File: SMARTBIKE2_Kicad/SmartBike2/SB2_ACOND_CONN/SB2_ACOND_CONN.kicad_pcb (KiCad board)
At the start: 2 copper layers, 45 x 100 mm, 30 parts, among them IC1 ESP32-WROVER-B__8MB_, J1 Conn_01x02, J2 Conn_01x01, J3 Conn_02x03_Counter_Clockwise, J4 Conn_01x04, J5 Conn_01x05, J6 Conn_01x08, J7 Conn_01x08, J8 Conn_01x04, SW1 SW_Boot, SW2 SW_Reset

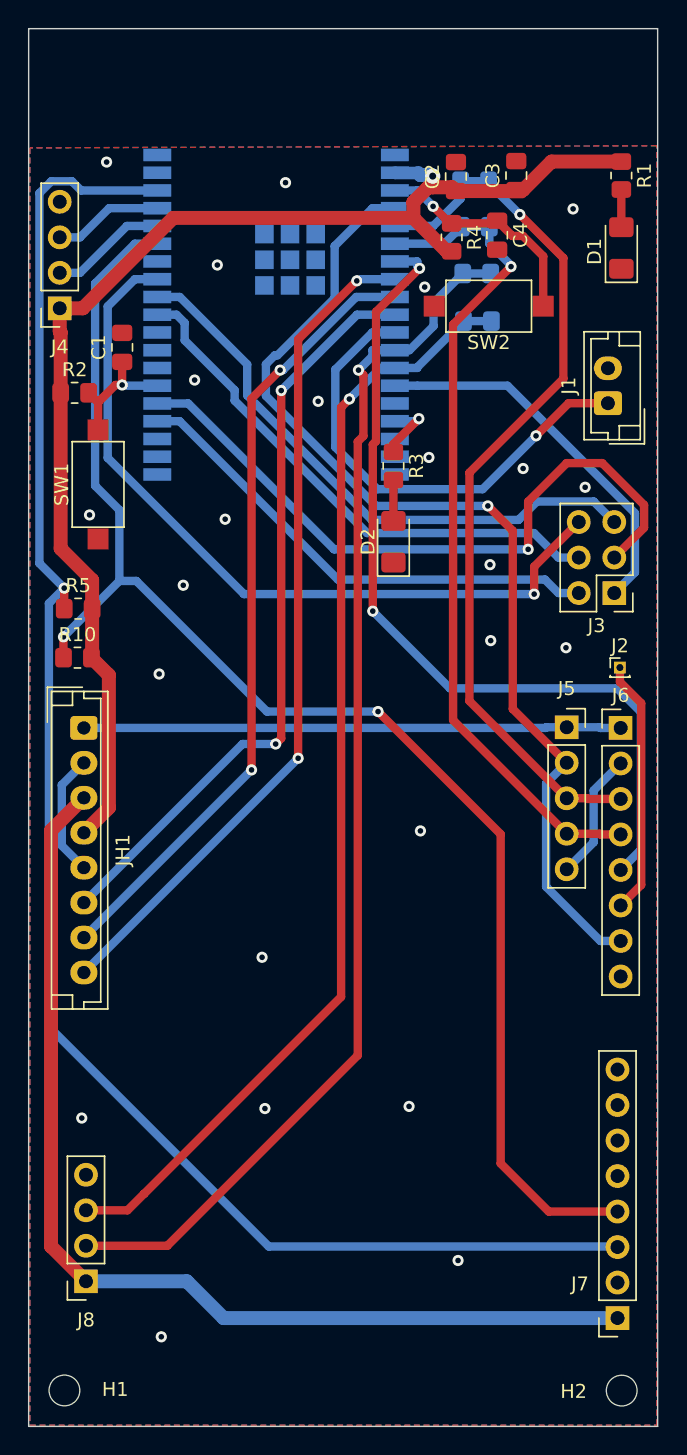
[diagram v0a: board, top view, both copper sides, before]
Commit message: Impresión vías sin metalización
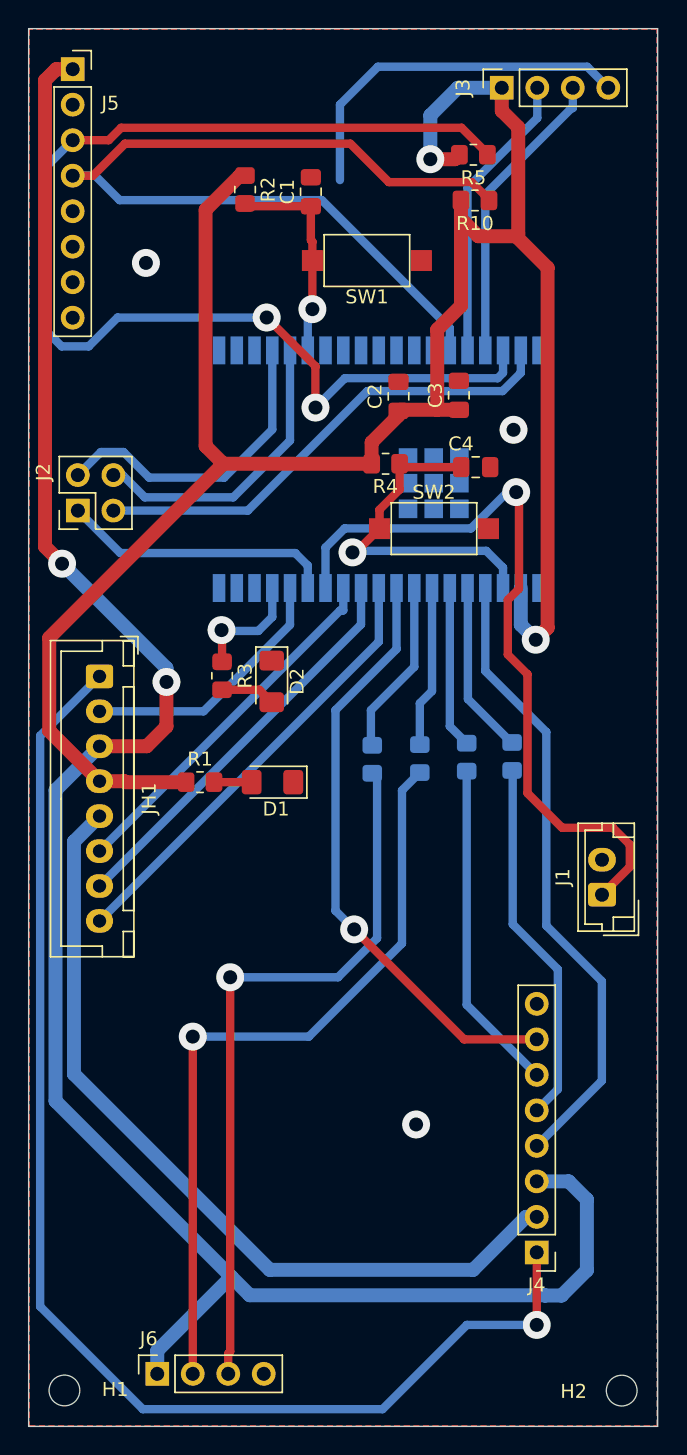
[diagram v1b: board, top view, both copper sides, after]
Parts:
- removed the J3 at (91.9, 65.4)
- removed the J5 at (88.5, 75.0)
- removed the J6 at (92.4, 75.0)
- added J4: Conn_01x08, Connector_PinHeader_2.54mm:PinHeader_1x08_P2.54mm_Vertical, F.Cu at (86.3, 112.5)
- J2: value Conn_01x01 -> Conn_02x02_Counter_Clockwise; footprint Connector_PinHeader_1.00mm:PinHeader_1x01_P1.00mm_Vertical -> Connector_PinHeader_2.54mm:PinHeader_2x02_P2.54mm_Vertical
- JH1: footprint Connector_JST:JST_EH_B8B-EH-A_1x08_P2.50mm_Vertical -> Connector_JST:JST_XH_B8B-XH-A_1x08_P2.50mm_Vertical
- moved J5 97.5 mm to (53.1, 27.9), turned to 0 degrees
- moved R1 52.8 mm to (62.3, 78.9), turned to 0 degrees
- moved D1 45.6 mm to (67.4, 78.9), turned to 180 degrees
- moved R10 43.3 mm to (81.9, 37.3), turned to 180 degrees
- moved R5 43.1 mm to (81.8, 34.0), turned to 180 degrees
- moved R6 41.2 mm to (84.6, 77.1), turned to -90 degrees
- moved J2 40.4 mm to (53.5, 59.5), turned to 90 degrees
- moved R7 38.0 mm to (81.3, 77.1), turned to -90 degrees
- moved J3 35.3 mm to (83.8, 29.2), turned to 90 degrees
- moved J1 35.2 mm to (91.0, 87.0)
- moved R8 34.9 mm to (78.0, 77.2), turned to -90 degrees
- moved R9 32.2 mm to (74.6, 77.3), turned to -90 degrees
- moved SW1 25.0 mm to (74.2, 41.6), turned to 180 degrees
- moved R3 19.4 mm to (63.8, 71.3)
- moved R2 19.0 mm to (65.5, 36.5), turned to -90 degrees
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- renumbered J4 to J3, J7 to J5, J8 to J6
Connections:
- IC1 pad 10: /Acondicionamiento/CtrGPSAc -> /Acondicionamiento/CtrAl
- IC1 pad 11: /Acondicionamiento/CtrLuces -> /Acondicionamiento/CtrSIM
- IC1 pad 12: /Acondicionamiento/TX_GPS -> /Acondicionamiento/CtrGPSAc
- IC1 pad 13: /Acondicionamiento/RX_GPS -> /Acondicionamiento/CtrLuces
- IC1 pad 29: /Acondicionamiento/MP4 -> unconnected-(IC1-IO5-Pad29)
- IC1 pad 30: /Acondicionamiento/MP5 -> unconnected-(IC1-IO18-Pad30)
- IC1 pad 31: /Acondicionamiento/MP6 -> unconnected-(IC1-IO19-Pad31)
- IC1 pad 37: unconnected-(IC1-IO23-Pad37) -> /Acondicionamiento/MP4
- IC1 pad 5: /Acondicionamiento/TX_SIM -> /Acondicionamiento/TX_SIM_1
- IC1 pad 6: /Acondicionamiento/RX_SIM -> /Acondicionamiento/RX_SIM_1
- IC1 pad 7: /Acondicionamiento/NE_SIM -> /Acondicionamiento/TX_GPS_1
- IC1 pad 8: /Acondicionamiento/CtrAl -> /Acondicionamiento/RX_GPS_1
- IC1 pad 9: /Acondicionamiento/CtrSIM -> /Acondicionamiento/GPIO_SIM
- J2 pad 1: /VdoSIM -> /Acondicionamiento/MP1
- JH1 pad 5: GND -> +5V
- R6 pad 1: /Acondicionamiento/TX_SIM -> /Acondicionamiento/TX_SIM_1
- R7 pad 1: /Acondicionamiento/RX_SIM -> /Acondicionamiento/RX_SIM_1
- R8 pad 1: /Acondicionamiento/TX_GPS -> /Acondicionamiento/TX_GPS_1
- R9 pad 1: /Acondicionamiento/RX_GPS -> /Acondicionamiento/RX_GPS_1
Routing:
- net +3.3_2: track 75.1 -> 147.1 mm, vias 0 -> 2
- net +3.3V: track 92.5 -> 155.9 mm, vias 1 -> 2
- net /Acondicionamiento/NE_SIM: track 62.1 -> 0.00 mm, vias 2 -> 0
- net +5V: track 0.00 -> 59.7 mm
- net /Acondicionamiento/MP6: track 56.2 -> 0.00 mm, vias 1 -> 0
- net 4.1V: track 38.4 -> 93.1 mm, vias 0 -> 1
- net /Acondicionamiento/GPIO_SIM: track 0.00 -> 43.1 mm, vias 0 -> 1
- net /Acondicionamiento/MP5: track 41.8 -> 0.00 mm
- net /Acondicionamiento/TX_SIM: track 64.7 -> 26.4 mm, vias 1 -> 0
- net /Acondicionamiento/SDA: track 102.9 -> 65.6 mm, vias 2 -> 0
- net /Acondicionamiento/RX_SIM: track 60.3 -> 23.8 mm, vias 1 -> 0
- net /Acondicionamiento/TX_GPS: track 88.0 -> 54.6 mm
- net /Acondicionamiento/SCL: track 118.6 -> 86.3 mm, vias 1 -> 2
- net /Acondicionamiento/RST_SIM: track 74.6 -> 45.3 mm, vias 1 -> 0
- net /Acondicionamiento/CtrAl: track 60.3 -> 32.1 mm, vias 2 -> 0
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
